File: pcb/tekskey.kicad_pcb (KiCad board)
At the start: 2 copper layers, 123.8 x 128.6 mm, 135 parts, among them J1 Conn_01x08, J2 Conn_01x08, SW0 MX_SW_HS, SW1 MX_SW_HS, SW10 MX_SW_HS, SW11 MX_SW_HS, SW12 MX_SW_HS, SW13 MX_SW_HS, SW14 MX_SW_HS, SW15 MX_SW_HS, SW1B1 MX_SW_HS, SW2 MX_SW_HS, SW20 MX_SW_HS, SW21 MX_SW_HS, SW22 MX_SW_HS, SW23 MX_SW_HS, SW24 MX_SW_HS, SW25 MX_SW_HS, SW2B1 MX_SW_HS, SW3 MX_SW_HS, SW30 MX_SW_HS, SW31 MX_SW_HS, SW32 MX_SW_HS, SW33 MX_SW_HS, SW34 MX_SW_HS, SW35 MX_SW_HS, SW3B1 MX_SW_HS, SW4 MX_SW_HS, SW40 MX_SW_HS, SW41 MX_SW_HS, SW42 MX_SW_HS, SW43 MX_SW_HS, SW44 MX_SW_HS, SW45 MX_SW_HS, SW4B1 MX_SW_HS, SW5 MX_SW_HS, SW50 MX_SW_HS, SW51 MX_SW_HS, SW51B1 MX_SW_HS, SW52 MX_SW_HS, SW53 MX_SW_HS, SW54 MX_SW_HS, SW55 MX_SW_HS, SW55B1 MX_SW_HS, SW5B1 MX_SW_HS

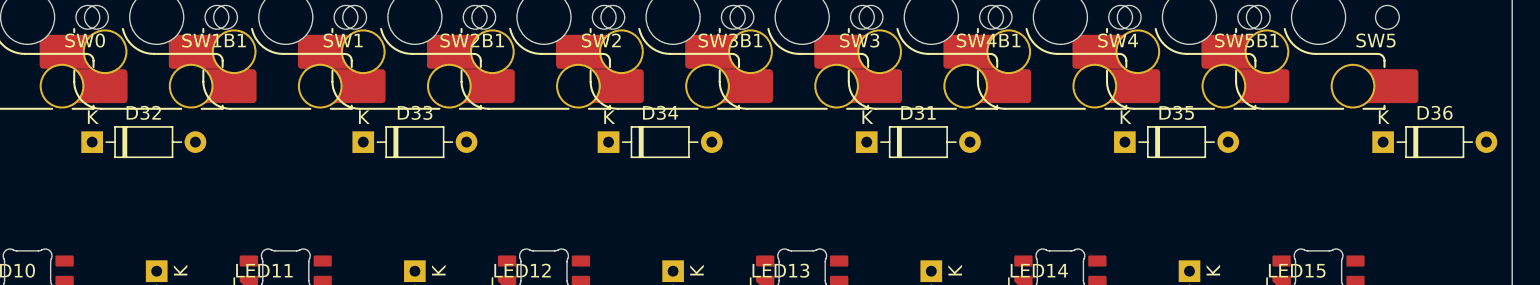
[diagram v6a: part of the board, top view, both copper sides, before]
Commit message: fix diode assignment
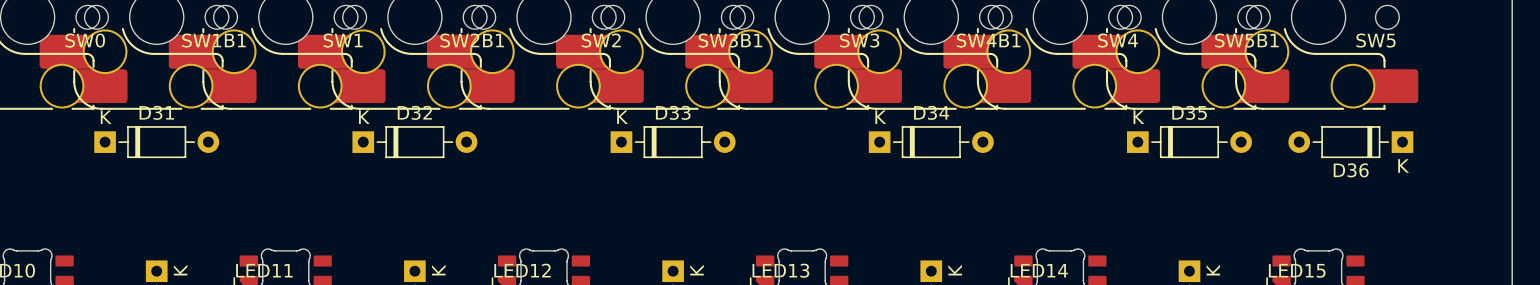
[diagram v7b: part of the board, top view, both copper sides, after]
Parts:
- moved D31 56.2 mm to (53.3, 47.6)
- moved D32 20.0 mm to (72.4, 47.6)
- moved D34 20.0 mm to (110.5, 47.6)
- moved D33 19.0 mm to (91.4, 47.6)
- moved D36 1.43 mm to (149.1, 47.6), turned to 180 degrees
- moved D35 0.95 mm to (129.5, 47.6)
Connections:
- SW1B1 pad 1: Net-(D32-Pad1) -> Net-(D31-Pad1)
- SW2B1 pad 1: Net-(D33-Pad1) -> Net-(D32-Pad1)
- SW3B1 pad 1: Net-(D34-Pad1) -> Net-(D33-Pad1)
- SW4B1 pad 1: Net-(D35-Pad1) -> Net-(D34-Pad1)
- SW5B1 pad 1: Net-(D36-Pad1) -> Net-(D35-Pad1)
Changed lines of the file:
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@@
   )
   (footprint "Diode_THT:D_DO-35_SOD27_P7.62mm_Horizontal" (layer "F.Cu")
-    (at 52.3875 47.625)
+    (at 72.39 47.625)
     (descr "Diode, DO-35_SOD27 series, Axial, Horizontal, pin pitch=7.62mm, , length*diameter=4*2mm^2, , http://www.diodes.com/_files/packages/DO-35.pdf")
     (tags "Diode DO-35_SOD27 series Axial Horizontal pin pitch 7.62mm  length 4mm diameter 2mm")
@@
   )
   (footprint "Diode_THT:D_DO-35_SOD27_P7.62mm_Horizontal" (layer "F.Cu")
-    (at 147.6375 47.625)
+    (at 149.06625 47.625 180)
     (descr "Diode, DO-35_SOD27 series, Axial, Horizontal, pin pitch=7.62mm, , length*diameter=4*2mm^2, , http://www.diodes.com/_files/packages/DO-35.pdf")
     (tags "Diode DO-35_SOD27 series Axial Horizontal pin pitch 7.62mm  length 4mm diameter 2mm")
@@
     (fp_line (start 7.62 0) (end 5.81 0) (layer "F.Fab") (width 0.1))
     (fp_line (start 2.31 -1) (end 2.31 1) (layer "F.Fab") (width 0.1))
-    (pad "1" thru_hole rect (at 0 0) (size 1.6 1.6) (drill 0.8) (layers *.Cu *.Mask)
+    (pad "1" thru_hole rect (at 0 0 180) (size 1.6 1.6) (drill 0.8) (layers *.Cu *.Mask)
       (net 75 "Net-(D36-Pad1)") (pinfunction "K") (pintype "passive"))
-    (pad "2" thru_hole oval (at 7.62 0) (size 1.6 1.6) (drill 0.8) (layers *.Cu *.Mask)
+    (pad "2" thru_hole oval (at 7.62 0 180) (size 1.6 1.6) (drill 0.8) (layers *.Cu *.Mask)
       (net 3 "row0") (pinfunction "A") (pintype "passive"))
     (model "${KICAD6_3DMODEL_DIR}/Diode_THT.3dshapes/D_DO-35_SOD27_P7.62mm_Horizontal.wrl"
@@
     (pad "" np_thru_hole circle (at 5.08 0 180) (size 1.75 1.75) (drill 1.75) (layers *.Cu *.Mask))
     (pad "1" smd rect (at 5.635 -2.54) (size 1.65 2.5) (layers "F.Cu")
-      (net 73 "Net-(D34-Pad1)") (pinfunction "1") (pintype "passive"))
+      (net 72 "Net-(D33-Pad1)") (pinfunction "1") (pintype "passive"))
     (pad "1" smd roundrect (at 7.36 -2.54 180) (size 2.55 2.5) (layers "F.Cu" "F.Paste" "F.Mask") (roundrect_rratio 0.1)
-      (net 73 "Net-(D34-Pad1)") (pinfunction "1") (pintype "passive"))
+      (net 72 "Net-(D33-Pad1)") (pinfunction "1") (pintype "passive"))
     (pad "1" thru_hole circle (at 3.81 -2.54 180) (size 3.3 3.3) (drill 3) (layers *.Cu *.Mask)
-      (net 73 "Net-(D34-Pad1)") (pinfunction "1") (pintype "passive"))
+      (net 72 "Net-(D33-Pad1)") (pinfunction "1") (pintype "passive"))
     (pad "2" thru_hole circle (at -2.54 -5.08 180) (size 3.3 3.3) (drill 3) (layers *.Cu *.Mask)
       (net 6 "col3") (pinfunction "2") (pintype "passive"))
@@
     (pad "" np_thru_hole circle (at -5.08 0 180) (size 1.75 1.75) (drill 1.75) (layers *.Cu *.Mask))
     (pad "1" thru_hole circle (at 3.81 -2.54 180) (size 3.3 3.3) (drill 3) (layers *.Cu *.Mask)
-      (net 72 "Net-(D33-Pad1)") (pinfunction "1") (pintype "passive"))
+      (net 71 "Net-(D32-Pad1)") (pinfunction "1") (pintype "passive"))
     (pad "1" smd roundrect (at 7.36 -2.54 180) (size 2.55 2.5) (layers "F.Cu" "F.Paste" "F.Mask") (roundrect_rratio 0.1)
-      (net 72 "Net-(D33-Pad1)") (pinfunction "1") (pintype "passive"))
+      (net 71 "Net-(D32-Pad1)") (pinfunction "1") (pintype "passive"))
     (pad "1" smd rect (at 5.635 -2.54) (size 1.65 2.5) (layers "F.Cu")
-      (net 72 "Net-(D33-Pad1)") (pinfunction "1") (pintype "passive"))
+      (net 71 "Net-(D32-Pad1)") (pinfunction "1") (pintype "passive"))
     (pad "2" smd roundrect (at -6.09 -5.08 180) (size 2.55 2.5) (layers "F.Cu" "F.Paste" "F.Mask") (roundrect_rratio 0.1)
       (net 5 "col2") (pinfunction "2") (pintype "passive"))
@@
   )
   (footprint "Diode_THT:D_DO-35_SOD27_P7.62mm_Horizontal" (layer "F.Cu")
-    (at 128.5875 47.625)
+    (at 129.54 47.625)
     (descr "Diode, DO-35_SOD27 series, Axial, Horizontal, pin pitch=7.62mm, , length*diameter=4*2mm^2, , http://www.diodes.com/_files/packages/DO-35.pdf")
     (tags "Diode DO-35_SOD27 series Axial Horizontal pin pitch 7.62mm  length 4mm diameter 2mm")
@@
   )
   (footprint "Diode_THT:D_DO-35_SOD27_P7.62mm_Horizontal" (layer "F.Cu")
-    (at 90.4875 47.625)
+    (at 110.49 47.625)
     (descr "Diode, DO-35_SOD27 series, Axial, Horizontal, pin pitch=7.62mm, , length*diameter=4*2mm^2, , http://www.diodes.com/_files/packages/DO-35.pdf")
     (tags "Diode DO-35_SOD27 series Axial Horizontal pin pitch 7.62mm  length 4mm diameter 2mm")
@@
     (pad "" np_thru_hole circle (at -5.08 0 180) (size 1.75 1.75) (drill 1.75) (layers *.Cu *.Mask))
     (pad "1" smd rect (at 5.635 -2.54) (size 1.65 2.5) (layers "F.Cu")
-      (net 74 "Net-(D35-Pad1)") (pinfunction "1") (pintype "passive"))
+      (net 73 "Net-(D34-Pad1)") (pinfunction "1") (pintype "passive"))
     (pad "1" thru_hole circle (at 3.81 -2.54 180) (size 3.3 3.3) (drill 3) (layers *.Cu *.Mask)
-      (net 74 "Net-(D35-Pad1)") (pinfunction "1") (pintype "passive"))
+      (net 73 "Net-(D34-Pad1)") (pinfunction "1") (pintype "passive"))
     (pad "1" smd roundrect (at 7.36 -2.54 180) (size 2.55 2.5) (layers "F.Cu" "F.Paste" "F.Mask") (roundrect_rratio 0.1)
-      (net 74 "Net-(D35-Pad1)") (pinfunction "1") (pintype "passive"))
+      (net 73 "Net-(D34-Pad1)") (pinfunction "1") (pintype "passive"))
     (pad "2" smd roundrect (at -6.09 -5.08 180) (size 2.55 2.5) (layers "F.Cu" "F.Paste" "F.Mask") (roundrect_rratio 0.1)
       (net 12 "col4") (pinfunction "2") (pintype "passive"))
@@
   )
   (footprint "Diode_THT:D_DO-35_SOD27_P7.62mm_Horizontal" (layer "F.Cu")
-    (at 109.5375 47.625)
+    (at 53.34 47.625)
     (descr "Diode, DO-35_SOD27 series, Axial, Horizontal, pin pitch=7.62mm, , length*diameter=4*2mm^2, , http://www.diodes.com/_files/packages/DO-35.pdf")
     (tags "Diode DO-35_SOD27 series Axial Horizontal pin pitch 7.62mm  length 4mm diameter 2mm")
@@
     (pad "" np_thru_hole circle (at 5.08 0 180) (size 1.75 1.75) (drill 1.75) (layers *.Cu *.Mask))
     (pad "1" smd rect (at 5.635 -2.54) (size 1.65 2.5) (layers "F.Cu")
-      (net 71 "Net-(D32-Pad1)") (pinfunction "1") (pintype "passive"))
+      (net 70 "Net-(D31-Pad1)") (pinfunction "1") (pintype "passive"))
     (pad "1" thru_hole circle (at 3.81 -2.54 180) (size 3.3 3.3) (drill 3) (layers *.Cu *.Mask)
-      (net 71 "Net-(D32-Pad1)") (pinfunction "1") (pintype "passive"))
+      (net 70 "Net-(D31-Pad1)") (pinfunction "1") (pintype "passive"))
     (pad "1" smd roundrect (at 7.36 -2.54 180) (size 2.55 2.5) (layers "F.Cu" "F.Paste" "F.Mask") (roundrect_rratio 0.1)
-      (net 71 "Net-(D32-Pad1)") (pinfunction "1") (pintype "passive"))
+      (net 70 "Net-(D31-Pad1)") (pinfunction "1") (pintype "passive"))
     (pad "2" smd roundrect (at -6.09 -5.08 180) (size 2.55 2.5) (layers "F.Cu" "F.Paste" "F.Mask") (roundrect_rratio 0.1)
       (net 4 "col1") (pinfunction "2") (pintype "passive"))
@@
   )
   (footprint "Diode_THT:D_DO-35_SOD27_P7.62mm_Horizontal" (layer "F.Cu")
-    (at 72.39 47.625)
+    (at 91.44 47.625)
     (descr "Diode, DO-35_SOD27 series, Axial, Horizontal, pin pitch=7.62mm, , length*diameter=4*2mm^2, , http://www.diodes.com/_files/packages/DO-35.pdf")
     (tags "Diode DO-35_SOD27 series Axial Horizontal pin pitch 7.62mm  length 4mm diameter 2mm")
@@
       (effects (font (size 1 1) (thickness 0.15)))
     )
-    (fp_text user "${REFERENCE}" (at 4.11 0) (layer "F.Fab")
+    (fp_text user "${REFERENCE}" (at 3.81 0) (layer "F.Fab")
       (effects (font (size 0.8 0.8) (thickness 0.12)))
     )
@@
     (pad "" np_thru_hole circle (at 5.08 0 180) (size 1.75 1.75) (drill 1.75) (layers *.Cu *.Mask))
     (pad "1" smd roundrect (at 7.36 -2.54 180) (size 2.55 2.5) (layers "F.Cu" "F.Paste" "F.Mask") (roundrect_rratio 0.1)
-      (net 75 "Net-(D36-Pad1)") (pinfunction "1") (pintype "passive"))
+      (net 74 "Net-(D35-Pad1)") (pinfunction "1") (pintype "passive"))
     (pad "1" smd rect (at 5.635 -2.54) (size 1.65 2.5) (layers "F.Cu")
-      (net 75 "Net-(D36-Pad1)") (pinfunction "1") (pintype "passive"))
+      (net 74 "Net-(D35-Pad1)") (pinfunction "1") (pintype "passive"))
     (pad "1" thru_hole circle (at 3.81 -2.54 180) (size 3.3 3.3) (drill 3) (layers *.Cu *.Mask)
-      (net 75 "Net-(D36-Pad1)") (pinfunction "1") (pintype "passive"))
+      (net 74 "Net-(D35-Pad1)") (pinfunction "1") (pintype "passive"))
     (pad "2" smd rect (at -4.34 -5.08 180) (size 1.65 2.5) (layers "F.Cu")
       (net 9 "col5") (pinfunction "2") (pintype "passive"))

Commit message: cleanup routing
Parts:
- removed JP1, JP10, JP11, JP2, JP3, JP4, JP5, JP6, JP7, JP8, JP9: Jumper_2_Open, Jumper:SolderJumper-2_P1.3mm_Open_Pad1.0x1.5mm
- moved J2 122.2 mm to (91.3, 25.4)
- moved J1 4.83 mm to (158.8, 72.9)
- moved D10 3.81 mm to (95.2, 72.4)
- moved D11 3.81 mm to (114.3, 72.4)
- moved D12 3.81 mm to (133.3, 72.4)
- moved D13 3.81 mm to (76.2, 91.4)
- moved D14 3.81 mm to (38.1, 91.4)
- moved D15 3.81 mm to (57.1, 91.4)
- moved D16 3.81 mm to (95.2, 91.4)
- moved D17 3.81 mm to (114.3, 91.4)
- moved D18 3.81 mm to (133.3, 91.4)
- moved D19 3.81 mm to (38.1, 110.5)
- moved D20 3.81 mm to (57.1, 110.5)
- moved D21 3.81 mm to (76.2, 110.5)
- moved D22 3.81 mm to (95.2, 110.5)
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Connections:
- D30 pad 2: Net-(D30-Pad2) -> Net-(SW55B1-Pad2)
- J1 pad 7: unconnected-(J1-Pad7) -> +5V
- J1 pad 8: unconnected-(J1-Pad8) -> GND
- J2 pad 7: unconnected-(J2-Pad7) -> LEDIN
- LED50 pad 2: Net-(LED50-Pad2) -> Net-(LED6-Pad3)
- LED51 pad 3: Net-(LED50-Pad2) -> Net-(LED6-Pad2)
- LED54 pad 2: Net-(LED54-Pad2) -> Net-(LED7-Pad3)
- LED55 pad 2: LEDOUT -> unconnected-(LED55-Pad2)
- LED55 pad 3: Net-(LED54-Pad2) -> Net-(LED55-Pad3)
- LED6 pad 2: Net-(LED51-Pad2) -> Net-(LED6-Pad2)
- LED6 pad 3: Net-(LED40-Pad2) -> Net-(LED6-Pad3)
- LED7 pad 2: LEDOUT -> Net-(LED55-Pad3)
- LED7 pad 3: Net-(LED53-Pad2) -> Net-(LED7-Pad3)
- SW51B1 pad 1: Net-(D26-Pad2) -> row5
- SW51B1 pad 2: row5 -> Net-(D26-Pad2)
- SW55 pad 1: Net-(D30-Pad2) -> Net-(SW55B1-Pad2)
- SW55B1 pad 1: Net-(D30-Pad2) -> row5
- SW55B1 pad 2: row5 -> Net-(SW55B1-Pad2)
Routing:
- net GND: track 0.00 -> 1046.9 mm
- net +5V: track 0.00 -> 989.1 mm
- net row5: track 0.00 -> 176.0 mm
- net col5: track 0.00 -> 159.1 mm
- net col0: track 0.00 -> 157.9 mm
- net col1: track 0.00 -> 152.4 mm
- net row4: track 0.00 -> 140.4 mm
- net row0: track 0.00 -> 134.7 mm
- net row3: track 0.00 -> 125.7 mm
- net col4: track 0.00 -> 124.5 mm
- net col2: track 0.00 -> 123.2 mm
- net col3: track 0.00 -> 113.4 mm
- net row2: track 0.00 -> 112.1 mm
- net row1: track 0.00 -> 111.9 mm
- net LEDIN: track 0.00 -> 52.5 mm
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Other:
- board size 123.8 x 128.6 mm -> 128.6 x 128.6 mm
